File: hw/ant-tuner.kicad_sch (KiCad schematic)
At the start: 4 parts, among them K701 G2RL-2, K702 G2RL-2, K703 G2RL-2

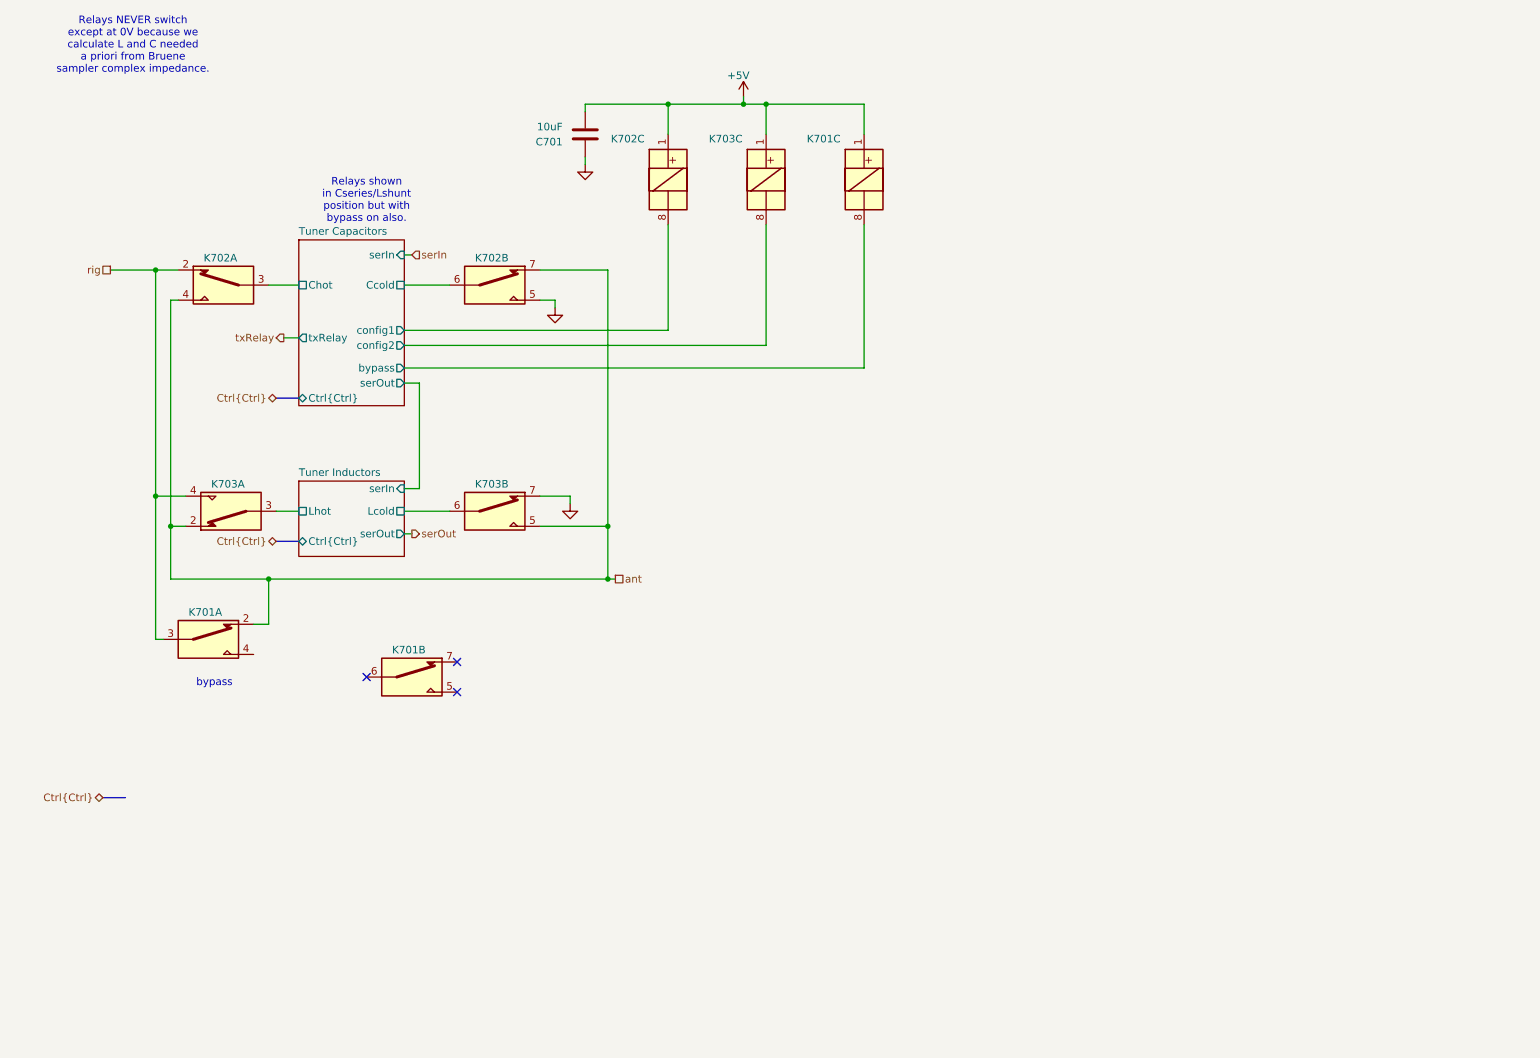
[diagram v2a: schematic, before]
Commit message: Have to use 5V signaling for relay drivers (ick). Add level shifter for that too. STM32 pins were way out of control. I think I got it all back together. Probably still need relay flyback snubber diodes in some places.
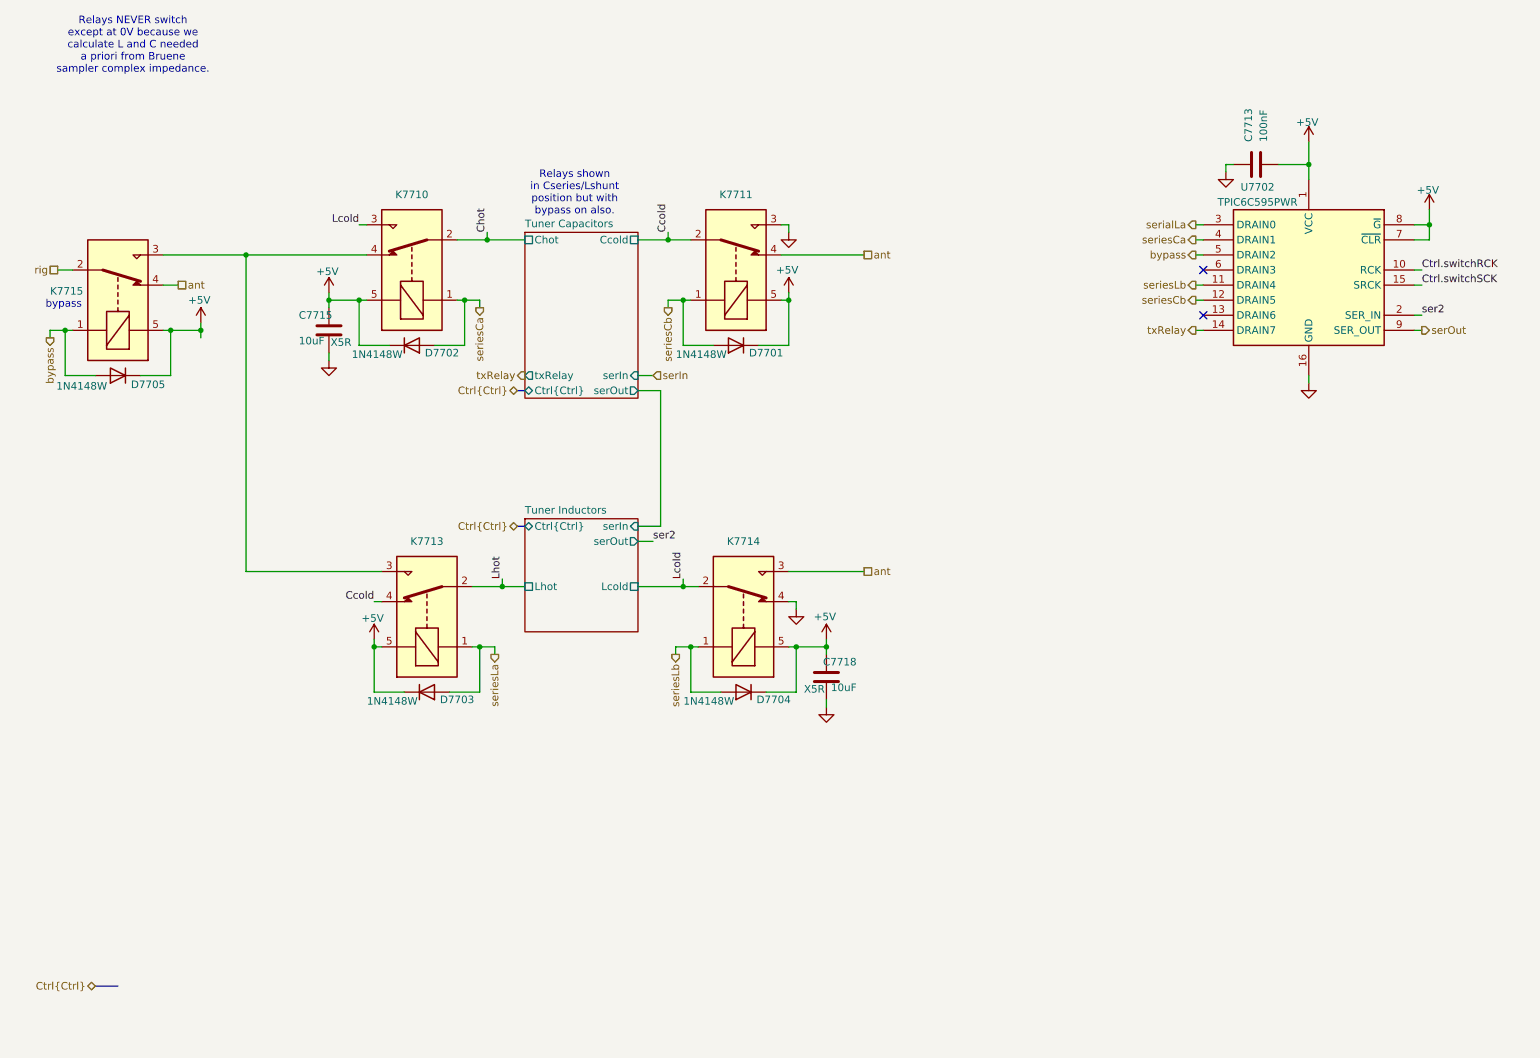
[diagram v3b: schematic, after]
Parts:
- removed C701: 10uF, Capacitor_SMD:C_1206_3216Metric, symbol Device:C
- removed K701, K702, K703: G2RL-2, Library:Relay_DPDT_Omron_G2RL-2, symbol Library:G2RL-2-functional
- added C7713: 100nF, Capacitor_SMD:C_0603_1608Metric, symbol Device:C
- added C7715, C7718: 10uF, Capacitor_SMD:C_0805_2012Metric, symbol Device:C
- added D7701, D7702, D7703, D7704, D7705: 1N4148W, Diode_SMD:D_SOD-123, symbol Diode:1N4148W
- added K7710, K7711, K7713, K7714, K7715: G5Q-14-05, Relay_THT:Relay_SPDT_Omron-G5Q-1, symbol Relay:G5Q-1
- added U7702: TPIC6C595PWR, SOP65P640X120-16N, symbol Library:TPIC6C595PWR
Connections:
- net +5V: now also C7713.2, C7715.1, C7718.1, D7701.1 (K), D7702.1 (K), D7703.1 (K), D7704.1 (K), D7705.1 (K), K7710.5, K7711.5, K7713.5, K7714.5, K7715.5, U7702.1 (VCC), U7702.7 (~{CLR}), U7702.8 (~{G})
- net GND: now also C7713.1, C7715.2, C7718.2, K7711.3, K7714.4, U7702.16 (GND)
- net ant: now also K7711.4, K7714.3, K7715.4
- net rig: now also K7715.2
- net serOut: now also U7702.9 (SER_OUT)
- net txRelay: now also U7702.14 (DRAIN7)
- new net: K7710.4, K7713.3, K7715.3
- new net Ccold: K7711.2, K7713.4
- new net Chot: K7710.2
- new net Ctrl.switchRCK: U7702.10 (RCK)
- new net Ctrl.switchSCK: U7702.15 (SRCK)
- new net Lcold: K7710.3, K7714.2
- new net Lhot: K7713.2
- new net bypass: D7705.2 (A), K7715.1, U7702.5 (DRAIN2)
- new net ser2: U7702.2 (SER_IN)
- new net serialLa: U7702.3 (DRAIN0)
- new net seriesCa: D7702.2 (A), K7710.1, U7702.4 (DRAIN1)
- new net seriesCb: D7701.2 (A), K7711.1, U7702.12 (DRAIN5)
- new net seriesLa: D7703.2 (A), K7713.1
- new net seriesLb: D7704.2 (A), K7714.1, U7702.11 (DRAIN4)
- no-connect marks 3 -> 2
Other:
- sheet Tuner Capacitors ports: added none; removed bypass, config1, config2

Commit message: I think I have finished the relay conversion and 5V SPI I/O expander crap
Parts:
- renumbered C7715 to C7774, C7718 to C7775, C7713 to C7776, D7705 to D7702, D7702 to D7703, D7703 to D7704, D7701 to D7705, D7704 to D7706, K7715 to K7703, K7710 to K7704, K7713 to K7705, K7711 to K7706, K7714 to K7707, U7702 to U7711
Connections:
- net C8: now reaches U7711.13 (DRAIN6)
- no-connect marks 2 -> 1
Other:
- sheet Tuner Capacitors ports: added C8; removed txRelay

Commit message: Starting to build guanella transformers. Mostly converted to 1-2-1 tx, but FPGA still to do.
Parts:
- removed D7702: 1N4148W, Diode_SMD:D_SOD-123, symbol Diode:1N4148W
- removed K7703: G5Q-14-05, Relay_THT:Relay_SPDT_Omron-G5Q-1, symbol Relay:G5Q-1
- renumbered C7774 to C7782, C7775 to C7783, C7776 to C7784, K7704 to K7703, K7705 to K7704, K7706 to K7705, K7707 to K7706, U7711 to U7714
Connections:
- net rig: now also K7703.4, K7704.3
- net bypass: no longer names the net of U7714.5 (DRAIN2)
- no-connect marks 1 -> 2
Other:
- note added: "Bypass is achieved by deselecting all L and all C."
- note removed: "bypass"

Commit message: Checkpoint. FPGA is mostly done (need a check!). Working on new LPFs. Need inductor footprints and to fix a bunch of broken/missing footprints.
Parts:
- C7784: cap-type (none) -> X7R
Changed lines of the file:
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@@
 			)
 		)
-		(property "cap-type" ""
+		(property "cap-type" "X7R"
 			(at 220.98 43.18 0)
 			(effects

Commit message: OK I have part numbers for consolidated caps, resistors, inductors and all ICs are now Uxxx refdes.
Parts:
- C7793: renamed from C7782; footprint Capacitor_SMD:C_0805_2012Metric -> Capacitor_SMD:C_0603_1608Metric; Manufacturer_Name (none) -> Taoup Uidem; Manufacturer_Part_Number (none) -> 81-GXT155R71E223KE1D; Mouser Part Number (none) -> 963-MLAST168BB5106MT; working-voltage 10V -> 25V
- C7794: renamed from C7783; footprint Capacitor_SMD:C_0805_2012Metric -> Capacitor_SMD:C_0603_1608Metric; Manufacturer_Name (none) -> Taoup Uidem; Manufacturer_Part_Number (none) -> 81-GXT155R71E223KE1D; Mouser Part Number (none) -> 963-MLAST168BB5106MT; working-voltage 10V -> 25V
- C7795: renamed from C7784; Manufacturer_Name (none) -> Kemet; Manufacturer_Part_Number (none) -> C0805F104K1RACAUTO; Mouser Part Number (none) -> 80-C0805F104K1RAUTO; working-voltage 10V -> 50V
- renumbered U7714 to U7713
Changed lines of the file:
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@@
 		(dnp no)
 		(fields_autoplaced yes)
-		(property "Reference" "#PWR07834"
+		(property "Reference" "#PWR07856"
 			(at 215.9 50.8 0)
 			(effects
@@
 			(project "NexRig"
 				(path "/8ae46c04-d01a-4756-8774-512b694bfaff/2406d03c-531b-4eaf-8b4b-4b266b9d0f2b/99bbdde6-e23e-4e3f-9a6c-8b2d863ddc64"
-					(reference "#PWR07834")
+					(reference "#PWR07856")
 					(unit 1)
 				)
@@
 		(on_board yes)
 		(dnp no)
-		(property "Reference" "#PWR07837"
+		(property "Reference" "#PWR07859"
 			(at 250.19 54.61 0)
 			(effects
@@
 			(project "NexRig"
 				(path "/8ae46c04-d01a-4756-8774-512b694bfaff/2406d03c-531b-4eaf-8b4b-4b266b9d0f2b/99bbdde6-e23e-4e3f-9a6c-8b2d863ddc64"
-					(reference "#PWR07837")
+					(reference "#PWR07859")
 					(unit 1)
 				)
@@
 		(on_board yes)
 		(dnp no)
-		(property "Reference" "#PWR07826"
+		(property "Reference" "#PWR07848"
 			(at 64.77 68.58 0)
 			(effects
@@
 			(project "NexRig"
 				(path "/8ae46c04-d01a-4756-8774-512b694bfaff/2406d03c-531b-4eaf-8b4b-4b266b9d0f2b/99bbdde6-e23e-4e3f-9a6c-8b2d863ddc64"
-					(reference "#PWR07826")
+					(reference "#PWR07848")
 					(unit 1)
 				)
@@
 		(on_board yes)
 		(dnp no)
-		(property "Reference" "#PWR07835"
+		(property "Reference" "#PWR07857"
 			(at 229.87 43.18 0)
 			(effects
@@
 			(project "NexRig"
 				(path "/8ae46c04-d01a-4756-8774-512b694bfaff/2406d03c-531b-4eaf-8b4b-4b266b9d0f2b/99bbdde6-e23e-4e3f-9a6c-8b2d863ddc64"
-					(reference "#PWR07835")
+					(reference "#PWR07857")
 					(unit 1)
 				)
@@
 		(dnp no)
 		(fields_autoplaced yes)
-		(property "Reference" "#PWR07831"
+		(property "Reference" "#PWR07853"
 			(at 143.51 124.46 0)
 			(effects
@@
 			(project "NexRig"
 				(path "/8ae46c04-d01a-4756-8774-512b694bfaff/2406d03c-531b-4eaf-8b4b-4b266b9d0f2b/99bbdde6-e23e-4e3f-9a6c-8b2d863ddc64"
-					(reference "#PWR07831")
+					(reference "#PWR07853")
 					(unit 1)
 				)
@@
 		(on_board yes)
 		(dnp no)
-		(property "Reference" "C7783"
+		(property "Reference" "C7794"
 			(at 153.67 127 0)
 			(effects
@@
 			)
 		)
-		(property "Footprint" "Capacitor_SMD:C_0805_2012Metric"
+		(property "Footprint" "Capacitor_SMD:C_0603_1608Metric"
 			(at 147.6248 133.35 0)
 			(effects
@@
 			)
 		)
-		(property "working-voltage" "10V"
+		(property "working-voltage" "25V"
+			(at 148.59 129.54 0)
+			(effects
+				(font
+					(size 1.27 1.27)
+				)
+				(hide yes)
+			)
+		)
+		(property "Manufacturer_Name" "Taoup Uidem"
+			(at 148.59 129.54 0)
+			(effects
+				(font
+					(size 1.27 1.27)
+				)
+				(hide yes)
+			)
+		)
+		(property "Manufacturer_Part_Number" "81-GXT155R71E223KE1D"
+			(at 148.59 129.54 0)
+			(effects
+				(font
+					(size 1.27 1.27)
+				)
+				(hide yes)
+			)
+		)
+		(property "Mouser Part Number" "963-MLAST168BB5106MT"
 			(at 148.59 129.54 0)
 			(effects
@@
 			(project "NexRig"
 				(path "/8ae46c04-d01a-4756-8774-512b694bfaff/2406d03c-531b-4eaf-8b4b-4b266b9d0f2b/99bbdde6-e23e-4e3f-9a6c-8b2d863ddc64"
-					(reference "C7783")
+					(reference "C7794")
 					(unit 1)
 				)
@@
 		(on_board yes)
 		(dnp no)
-		(property "Reference" "#PWR07830"
+		(property "Reference" "#PWR07852"
 			(at 142.24 68.58 0)
 			(effects
@@
 			(project "NexRig"
 				(path "/8ae46c04-d01a-4756-8774-512b694bfaff/2406d03c-531b-4eaf-8b4b-4b266b9d0f2b/99bbdde6-e23e-4e3f-9a6c-8b2d863ddc64"
-					(reference "#PWR07830")
+					(reference "#PWR07852")
 					(unit 1)
 				)
@@
 		(dnp no)
 		(fields_autoplaced yes)
-		(property "Reference" "#PWR07836"
+		(property "Reference" "#PWR07858"
 			(at 229.87 86.36 0)
 			(effects
@@
 			(project "NexRig"
 				(path "/8ae46c04-d01a-4756-8774-512b694bfaff/2406d03c-531b-4eaf-8b4b-4b266b9d0f2b/99bbdde6-e23e-4e3f-9a6c-8b2d863ddc64"
-					(reference "#PWR07836")
+					(reference "#PWR07858")
 					(unit 1)
 				)
@@
 		(on_board yes)
 		(dnp no)
-		(property "Reference" "C7782"
+		(property "Reference" "C7793"
 			(at 59.69 68.58 0)
 			(effects
@@
 			)
 		)
-		(property "Footprint" "Capacitor_SMD:C_0805_2012Metric"
+		(property "Footprint" "Capacitor_SMD:C_0603_1608Metric"
 			(at 65.7352 74.93 0)
 			(effects
@@
 			)
 		)
-		(property "working-voltage" "10V"
+		(property "working-voltage" "25V"
+			(at 64.77 71.12 0)
+			(effects
+				(font
+					(size 1.27 1.27)
+				)
+				(hide yes)
+			)
+		)
+		(property "Manufacturer_Name" "Taoup Uidem"
+			(at 64.77 71.12 0)
+			(effects
+				(font
+					(size 1.27 1.27)
+				)
+				(hide yes)
+			)
+		)
+		(property "Manufacturer_Part_Number" "81-GXT155R71E223KE1D"
+			(at 64.77 71.12 0)
+			(effects
+				(font
+					(size 1.27 1.27)
+				)
+				(hide yes)
+			)
+		)
+		(property "Mouser Part Number" "963-MLAST168BB5106MT"
 			(at 64.77 71.12 0)
 			(effects
@@
 			(project "NexRig"
 				(path "/8ae46c04-d01a-4756-8774-512b694bfaff/2406d03c-531b-4eaf-8b4b-4b266b9d0f2b/99bbdde6-e23e-4e3f-9a6c-8b2d863ddc64"
-					(reference "C7782")
+					(reference "C7793")
 					(unit 1)
 				)
@@
 		(dnp no)
 		(fields_autoplaced yes)
-		(property "Reference" "#PWR07829"
+		(property "Reference" "#PWR07851"
 			(at 142.24 60.96 0)
 			(effects
@@
 			(project "NexRig"
 				(path "/8ae46c04-d01a-4756-8774-512b694bfaff/2406d03c-531b-4eaf-8b4b-4b266b9d0f2b/99bbdde6-e23e-4e3f-9a6c-8b2d863ddc64"
-					(reference "#PWR07829")
+					(reference "#PWR07851")
 					(unit 1)
 				)
@@
 		(on_board yes)
 		(dnp no)
-		(property "Reference" "#PWR07827"
+		(property "Reference" "#PWR07849"
 			(at 64.77 82.55 0)
 			(effects
@@
 			(project "NexRig"
 				(path "/8ae46c04-d01a-4756-8774-512b694bfaff/2406d03c-531b-4eaf-8b4b-4b266b9d0f2b/99bbdde6-e23e-4e3f-9a6c-8b2d863ddc64"
-					(reference "#PWR07827")
+					(reference "#PWR07849")
 					(unit 1)
 				)
@@
 		(on_board yes)
 		(dnp no)
-		(property "Reference" "#PWR07833"
+		(property "Reference" "#PWR07855"
 			(at 148.59 140.97 0)
 			(effects
@@
 			(project "NexRig"
 				(path "/8ae46c04-d01a-4756-8774-512b694bfaff/2406d03c-531b-4eaf-8b4b-4b266b9d0f2b/99bbdde6-e23e-4e3f-9a6c-8b2d863ddc64"
-					(reference "#PWR07833")
+					(reference "#PWR07855")
 					(unit 1)
 				)
@@
 		(on_board yes)
 		(dnp no)
-		(property "Reference" "#PWR07828"
+		(property "Reference" "#PWR07850"
 			(at 72.39 127 0)
 			(effects
@@
 			(project "NexRig"
 				(path "/8ae46c04-d01a-4756-8774-512b694bfaff/2406d03c-531b-4eaf-8b4b-4b266b9d0f2b/99bbdde6-e23e-4e3f-9a6c-8b2d863ddc64"
-					(reference "#PWR07828")
+					(reference "#PWR07850")
 					(unit 1)
 				)
@@
 		(on_board yes)
 		(dnp no)
-		(property "Reference" "C7784"
+		(property "Reference" "C7795"
 			(at 219.7099 39.37 0)
 			(effects
@@
 			)
 		)
-		(property "working-voltage" "10V"
+		(property "working-voltage" "50V"
 			(at 220.98 43.18 0)
 			(effects
@@
 					(size 1.27 1.27)
 				)
+			)
+		)
+		(property "Manufacturer_Name" "Kemet"
+			(at 220.98 43.18 0)
+			(effects
+				(font
+					(size 1.27 1.27)
+				)
+				(hide yes)
+			)
+		)
+		(property "Manufacturer_Part_Number" "C0805F104K1RACAUTO"
+			(at 220.98 43.18 0)
+			(effects
+				(font
+					(size 1.27 1.27)
+				)
+				(hide yes)
+			)
+		)
+		(property "Mouser Part Number" "80-C0805F104K1RAUTO"
+			(at 220.98 43.18 0)
+			(effects
+				(font
+					(size 1.27 1.27)
+				)
+				(hide yes)
 			)
 		)
@@
 			(project "NexRig"
 				(path "/8ae46c04-d01a-4756-8774-512b694bfaff/2406d03c-531b-4eaf-8b4b-4b266b9d0f2b/99bbdde6-e23e-4e3f-9a6c-8b2d863ddc64"
-					(reference "C7784")
+					(reference "C7795")
 					(unit 1)
 				)
@@
 		(on_board yes)
 		(dnp no)
-		(property "Reference" "#PWR07832"
+		(property "Reference" "#PWR07854"
 			(at 148.59 127 0)
 			(effects
@@
 			(project "NexRig"
 				(path "/8ae46c04-d01a-4756-8774-512b694bfaff/2406d03c-531b-4eaf-8b4b-4b266b9d0f2b/99bbdde6-e23e-4e3f-9a6c-8b2d863ddc64"
-					(reference "#PWR07832")
+					(reference "#PWR07854")
 					(unit 1)
 				)
@@
 		(on_board yes)
 		(dnp no)
-		(property "Reference" "U7714"
+		(property "Reference" "U7713"
 			(at 221.234 46.99 0)
 			(effects
@@
 			(project "NexRig"
 				(path "/8ae46c04-d01a-4756-8774-512b694bfaff/2406d03c-531b-4eaf-8b4b-4b266b9d0f2b/99bbdde6-e23e-4e3f-9a6c-8b2d863ddc64"
-					(reference "U7714")
+					(reference "U7713")
 					(unit 1)
 				)
